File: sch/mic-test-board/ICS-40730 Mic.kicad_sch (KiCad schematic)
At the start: 2 parts, among them U4 ICS-40730

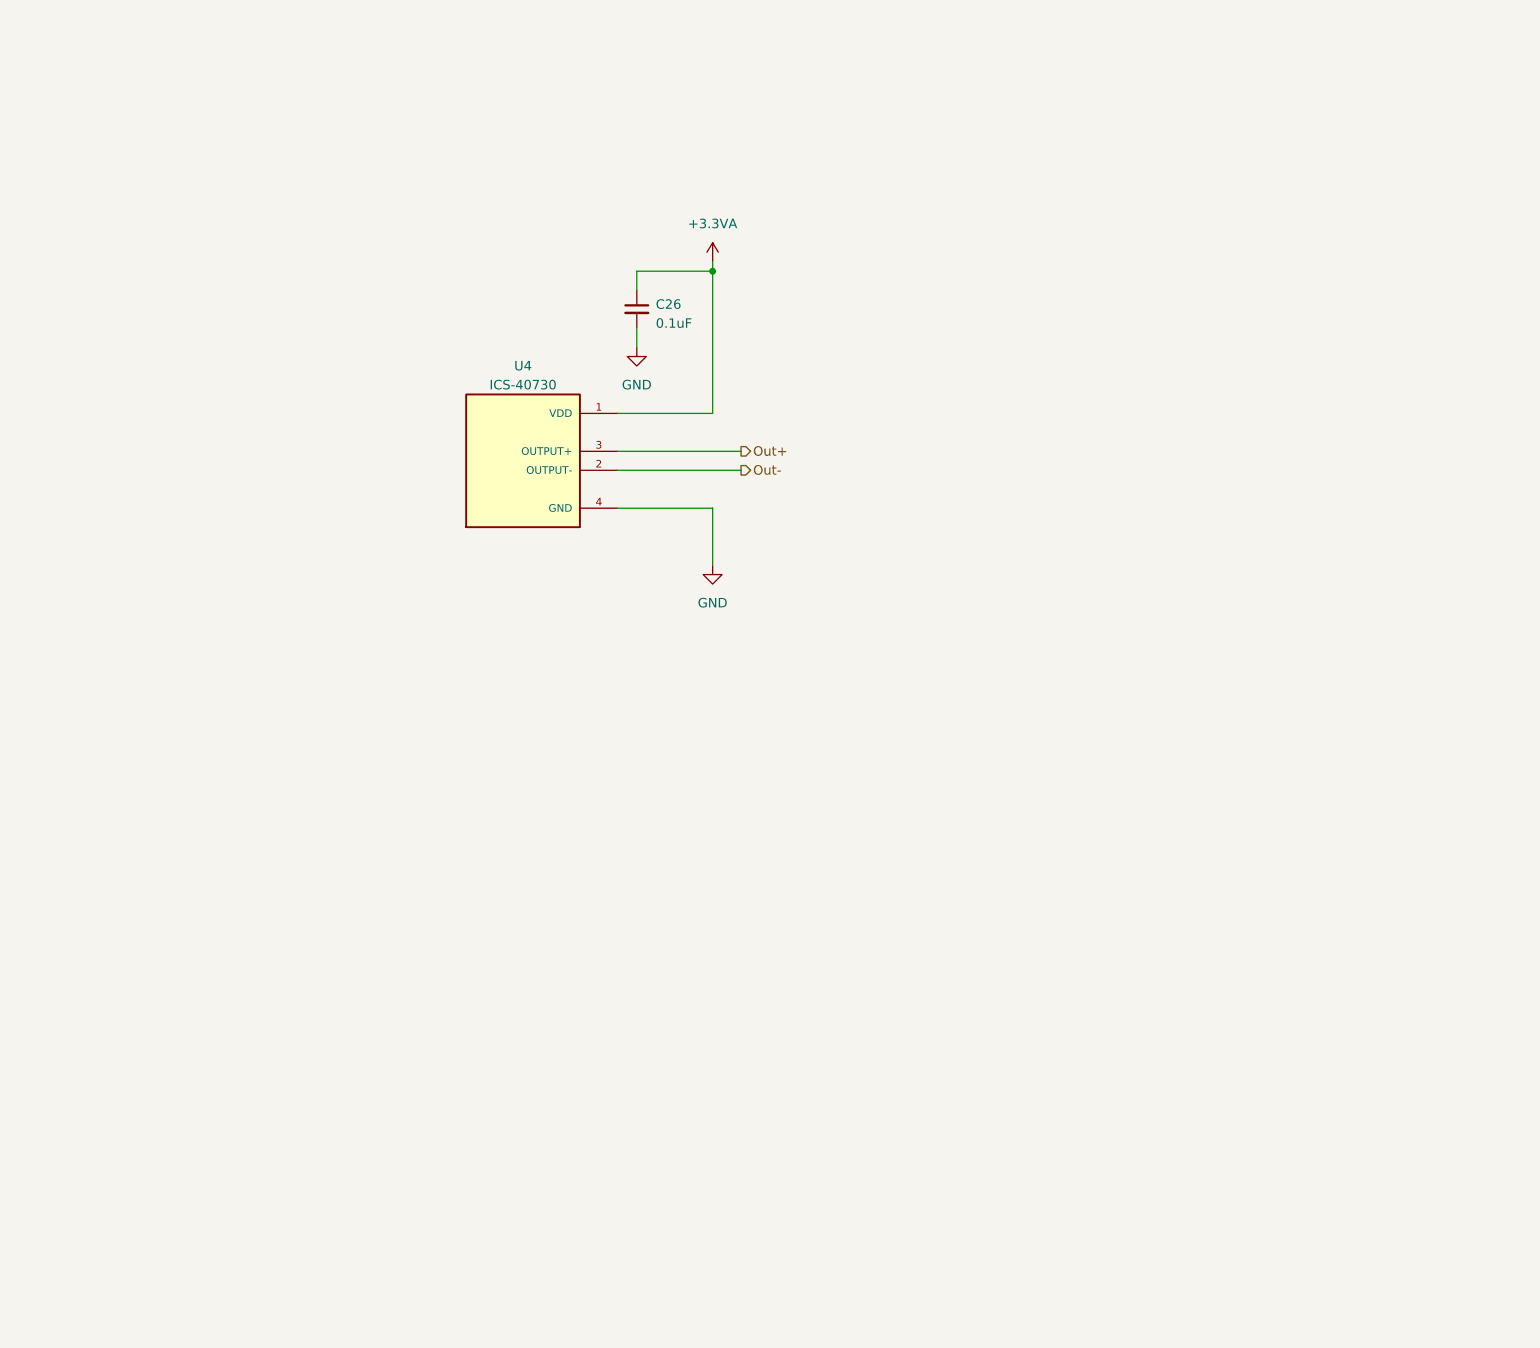
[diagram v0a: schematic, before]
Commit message: pcb: commit before large routing effort
 - schematic refactor to split preamps to each mic board
 - Mic board and main board are placed
 - no tracks laid
 - critical parts selected
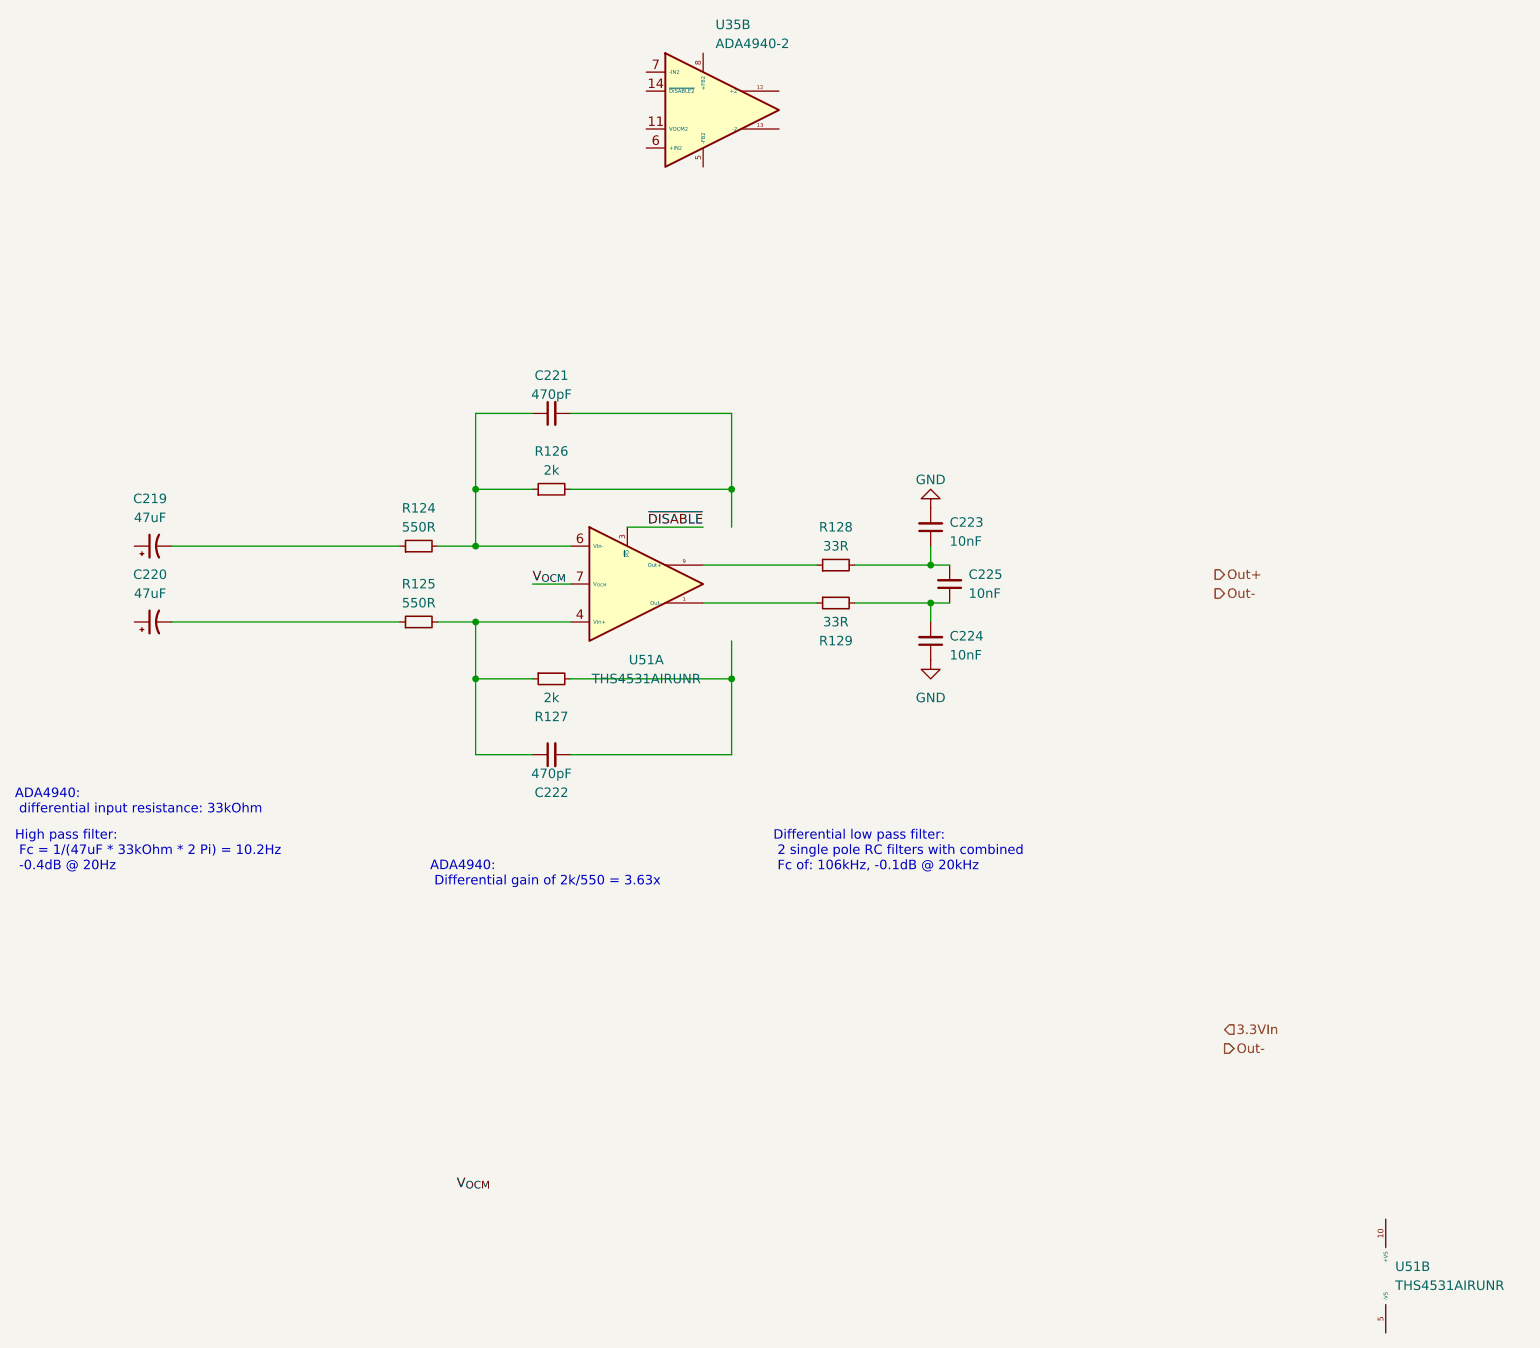
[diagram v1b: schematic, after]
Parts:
- removed C26: 0.1uF, Capacitor_SMD:C_0603_1608Metric, symbol Device:C_Small
- removed U4: ICS-40730, mic-test-board:MIC_ICS-40730, symbol mic-test-pcb:ICS-40730
- added C219, C220: 47uF, Capacitor_Tantalum_SMD:CP_EIA-1608-08_AVX-J, symbol Device:C_Polarized_Small_US
- added C221, C222: 470pF, Capacitor_SMD:C_0603_1608Metric, symbol Device:C_Small
- added C223, C224, C225: 10nF, Capacitor_SMD:C_0603_1608Metric, symbol Device:C_Small
- added R124, R125: 550R, Resistor_SMD:R_0603_1608Metric, symbol Device:R_Small
- added R126, R127: 2k, Resistor_SMD:R_0603_1608Metric, symbol Device:R_Small
- added R128, R129: 33R, Resistor_SMD:R_0603_1608Metric, symbol Device:R_Small
- added U35: ADA4940-2, Package_CSP:LFCSP-24-1EP_4x4mm_P0.5mm_EP2.5x2.5mm, symbol mic-test-pcb:ADA4940-2
- added U51: THS4531AIRUNR, Package_DFN_QFN:Texas_RUN0010A_WQFN-10_2x2mm_P0.5mm, symbol mic-test-pcb:THS4531AIRUNR
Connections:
- net GND: now also C223.2, C224.1
- new net: C221.1, R124.2, R126.1, U51.6 (VIn-)
- new net: C221.2, R126.2
- new net: R129.1, U51.1 (Out-)
- new net: C224.2, C225.1, R129.2
- new net: C219.2, R124.1
- new net: C220.2, R125.1
- new net: C222.1, R125.2, R127.1, U51.4 (Vin+)
- new net: C222.2, R127.2
- new net: R128.1, U51.9 (Out+)
- new net: C223.1, C225.2, R128.2
- new net V_{OCM}: U51.7 (V_{OCM})
- new net ~{DISABLE}: U51.3 (~{PD})
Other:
- note added: "ADA4940: Differential gain of 2k/550 = 3.63x"
- note added: "ADA4940: differential input resistance: 33kOhm"
- note added: "Differential low pass filter: 2 single pole RC filters with combined Fc of: 106kHz, -0.1dB @ 20kHz"
- note added: "High pass filter: Fc = 1/(47uF * 33kOhm * 2 Pi) = 10.2Hz -0.4dB @ 20Hz"
- company: (none) -> Josh Berry
- title: (none) -> Sound Compass POC
